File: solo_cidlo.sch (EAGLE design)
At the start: 4 parts, among them Q1 QRD1114

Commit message: Add files via upload
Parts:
- removed Q1: QRD1114, QRD1114:QRD1114
- added S1: QRD1114, QRD1114:QRD1114
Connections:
- removed net N$3: JP2.1, R1.2, R2.2
- removed net N$4: JP2.3, Q1.P$2, Q1.P$4
- new net +5V: JP2.2, R1.2, R2.2
- new net GND: JP2.3, S1.P$2, S1.P$4
- net N$1: now also S1.P$3; no longer Q1.P$3
- net N$2: now also JP2.1, S1.P$1; no longer JP2.2, Q1.P$1
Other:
- moved on the sheet: R1, R2
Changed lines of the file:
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@@
 <layers>
 <layer number="1" name="Top" color="4" fill="1" visible="no" active="no"/>
+<layer number="2" name="Route2" color="1" fill="3" visible="no" active="no"/>
+<layer number="3" name="Route3" color="4" fill="3" visible="no" active="no"/>
+<layer number="4" name="Route4" color="1" fill="4" visible="no" active="no"/>
+<layer number="5" name="Route5" color="4" fill="4" visible="no" active="no"/>
+<layer number="6" name="Route6" color="1" fill="8" visible="no" active="no"/>
+<layer number="7" name="Route7" color="4" fill="8" visible="no" active="no"/>
+<layer number="8" name="Route8" color="1" fill="2" visible="no" active="no"/>
+<layer number="9" name="Route9" color="4" fill="2" visible="no" active="no"/>
+<layer number="10" name="Route10" color="1" fill="7" visible="no" active="no"/>
+<layer number="11" name="Route11" color="4" fill="7" visible="no" active="no"/>
+<layer number="12" name="Route12" color="1" fill="5" visible="no" active="no"/>
+<layer number="13" name="Route13" color="4" fill="5" visible="no" active="no"/>
+<layer number="14" name="Route14" color="1" fill="6" visible="no" active="no"/>
+<layer number="15" name="Route15" color="4" fill="6" visible="no" active="no"/>
 <layer number="16" name="Bottom" color="1" fill="1" visible="no" active="no"/>
 <layer number="17" name="Pads" color="2" fill="1" visible="no" active="no"/>
@@
 </classes>
 <parts>
-<part name="Q1" library="QRD1114" deviceset="QRD1114" device=""/>
+<part name="S1" library="QRD1114" deviceset="QRD1114" device=""/>
 <part name="R1" library="resistor" library_urn="urn:adsk.eagle:library:348" deviceset="R-EU_" device="MELF0102W" package3d_urn="urn:adsk.eagle:package:26105/1" value="330"/>
 <part name="R2" library="resistor" library_urn="urn:adsk.eagle:library:348" deviceset="R-EU_" device="MELF0102W" package3d_urn="urn:adsk.eagle:package:26105/1" value="10 k"/>
 <part name="JP2" library="pinhead" library_urn="urn:adsk.eagle:library:325" deviceset="PINHD-1X3" device="" package3d_urn="urn:adsk.eagle:package:22458/2"/>
+<part name="GND1" library="supply1" library_urn="urn:adsk.eagle:library:371" deviceset="GND" device=""/>
+<part name="P+1" library="supply1" library_urn="urn:adsk.eagle:library:371" deviceset="+5V" device=""/>
 </parts>
 <sheets>
@@
 </plain>
 <instances>
-<instance part="Q1" gate="G$1" x="43.18" y="45.72"/>
-<instance part="R1" gate="G$1" x="40.64" y="63.5" rot="R90"/>
-<instance part="R2" gate="G$1" x="45.72" y="63.5" rot="R90"/>
+<instance part="S1" gate="G$1" x="43.18" y="38.1"/>
+<instance part="R1" gate="G$1" x="40.64" y="58.42" rot="R90"/>
+<instance part="R2" gate="G$1" x="45.72" y="58.42" rot="R90"/>
 <instance part="JP2" gate="A" x="43.18" y="81.28" rot="R90"/>
+<instance part="GND1" gate="1" x="58.42" y="73.66" rot="R90"/>
+<instance part="P+1" gate="1" x="33.02" y="66.04" rot="R90"/>
 </instances>
 <busses>
@@
 <net name="N$1" class="0">
 <segment>
-<pinref part="Q1" gate="G$1" pin="P$3"/>
+<pinref part="S1" gate="G$1" pin="P$3"/>
 <pinref part="R1" gate="G$1" pin="1"/>
-<wire x1="40.64" y1="55.88" x2="40.64" y2="58.42" width="0.1524" layer="91"/>
+<wire x1="40.64" y1="48.26" x2="40.64" y2="53.34" width="0.1524" layer="91"/>
 </segment>
 </net>
 <net name="N$2" class="0">
 <segment>
+<pinref part="S1" gate="G$1" pin="P$1"/>
+<wire x1="48.26" y1="48.26" x2="48.26" y2="50.8" width="0.1524" layer="91"/>
+<wire x1="48.26" y1="50.8" x2="48.26" y2="71.12" width="0.1524" layer="91"/>
 <pinref part="R2" gate="G$1" pin="1"/>
-<wire x1="45.72" y1="58.42" x2="48.26" y2="58.42" width="0.1524" layer="91"/>
-<pinref part="Q1" gate="G$1" pin="P$1"/>
-<wire x1="48.26" y1="58.42" x2="48.26" y2="55.88" width="0.1524" layer="91"/>
-<junction x="48.26" y="58.42"/>
-<wire x1="48.26" y1="58.42" x2="48.26" y2="71.12" width="0.1524" layer="91"/>
-<wire x1="48.26" y1="71.12" x2="43.18" y2="71.12" width="0.1524" layer="91"/>
-<pinref part="JP2" gate="A" pin="2"/>
-<wire x1="43.18" y1="71.12" x2="43.18" y2="78.74" width="0.1524" layer="91"/>
+<wire x1="45.72" y1="53.34" x2="45.72" y2="50.8" width="0.1524" layer="91"/>
+<wire x1="45.72" y1="50.8" x2="48.26" y2="50.8" width="0.1524" layer="91"/>
+<junction x="48.26" y="50.8"/>
+<pinref part="JP2" gate="A" pin="1"/>
+<wire x1="48.26" y1="71.12" x2="40.64" y2="71.12" width="0.1524" layer="91"/>
+<wire x1="40.64" y1="71.12" x2="40.64" y2="78.74" width="0.1524" layer="91"/>
 </segment>
 </net>
-<net name="N$3" class="0">
+<net name="GND" class="0">
 <segment>
-<pinref part="R1" gate="G$1" pin="2"/>
-<pinref part="R2" gate="G$1" pin="2"/>
-<wire x1="40.64" y1="68.58" x2="45.72" y2="68.58" width="0.1524" layer="91"/>
-<junction x="40.64" y="68.58"/>
-<pinref part="JP2" gate="A" pin="1"/>
-<wire x1="40.64" y1="68.58" x2="40.64" y2="78.74" width="0.1524" layer="91"/>
+<pinref part="S1" gate="G$1" pin="P$4"/>
+<wire x1="40.64" y1="27.94" x2="40.64" y2="25.4" width="0.1524" layer="91"/>
+<wire x1="40.64" y1="25.4" x2="48.26" y2="25.4" width="0.1524" layer="91"/>
+<wire x1="48.26" y1="25.4" x2="53.34" y2="25.4" width="0.1524" layer="91"/>
+<wire x1="53.34" y1="25.4" x2="53.34" y2="73.66" width="0.1524" layer="91"/>
+<wire x1="53.34" y1="73.66" x2="45.72" y2="73.66" width="0.1524" layer="91"/>
+<pinref part="S1" gate="G$1" pin="P$2"/>
+<wire x1="48.26" y1="27.94" x2="48.26" y2="25.4" width="0.1524" layer="91"/>
+<junction x="48.26" y="25.4"/>
+<pinref part="JP2" gate="A" pin="3"/>
+<wire x1="45.72" y1="73.66" x2="45.72" y2="78.74" width="0.1524" layer="91"/>
+<pinref part="GND1" gate="1" pin="GND"/>
+<wire x1="55.88" y1="73.66" x2="53.34" y2="73.66" width="0.1524" layer="91"/>
+<junction x="53.34" y="73.66"/>
 </segment>
 </net>
-<net name="N$4" class="0">
+<net name="+5V" class="0">
 <segment>
-<pinref part="Q1" gate="G$1" pin="P$4"/>
-<wire x1="40.64" y1="35.56" x2="40.64" y2="33.02" width="0.1524" layer="91"/>
-<wire x1="40.64" y1="33.02" x2="48.26" y2="33.02" width="0.1524" layer="91"/>
-<wire x1="48.26" y1="33.02" x2="53.34" y2="33.02" width="0.1524" layer="91"/>
-<wire x1="53.34" y1="33.02" x2="53.34" y2="73.66" width="0.1524" layer="91"/>
-<wire x1="53.34" y1="73.66" x2="45.72" y2="73.66" width="0.1524" layer="91"/>
-<pinref part="Q1" gate="G$1" pin="P$2"/>
-<wire x1="48.26" y1="35.56" x2="48.26" y2="33.02" width="0.1524" layer="91"/>
-<junction x="48.26" y="33.02"/>
-<pinref part="JP2" gate="A" pin="3"/>
-<wire x1="45.72" y1="73.66" x2="45.72" y2="78.74" width="0.1524" layer="91"/>
+<pinref part="JP2" gate="A" pin="2"/>
+<wire x1="43.18" y1="78.74" x2="43.18" y2="66.04" width="0.1524" layer="91"/>
+<wire x1="43.18" y1="66.04" x2="45.72" y2="66.04" width="0.1524" layer="91"/>
+<pinref part="R2" gate="G$1" pin="2"/>
+<wire x1="45.72" y1="66.04" x2="45.72" y2="63.5" width="0.1524" layer="91"/>
+<pinref part="R1" gate="G$1" pin="2"/>
+<wire x1="43.18" y1="66.04" x2="40.64" y2="66.04" width="0.1524" layer="91"/>
+<wire x1="40.64" y1="66.04" x2="40.64" y2="63.5" width="0.1524" layer="91"/>
+<junction x="43.18" y="66.04"/>
+<pinref part="P+1" gate="1" pin="+5V"/>
+<wire x1="35.56" y1="66.04" x2="40.64" y2="66.04" width="0.1524" layer="91"/>
+<junction x="40.64" y="66.04"/>
 </segment>
 </net>

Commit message: Add files via upload
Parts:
- added LED1: (no value), led:LEDCHIPLED_0603
- added R3: 330, resistor:R-EU_R0201
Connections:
- net N$1 renamed IL1
- net N$2 renamed S1
- new net KL1: LED1.A, R3.1
- net +5V: now also R3.2
- net GND: now also LED1.C
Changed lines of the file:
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@@
 <setting verticaltext="up"/>
 </settings>
-<grid distance="0.1" unitdist="inch" unit="inch" style="lines" multiple="1" display="yes" altdistance="0.01" altunitdist="inch" altunit="inch"/>
+<grid distance="0.1" unitdist="inch" unit="inch" style="lines" multiple="1" display="no" altdistance="0.01" altunitdist="inch" altunit="inch"/>
 <layers>
-<layer number="1" name="Top" color="4" fill="1" visible="no" active="no"/>
-<layer number="2" name="Route2" color="1" fill="3" visible="no" active="no"/>
-<layer number="3" name="Route3" color="4" fill="3" visible="no" active="no"/>
-<layer number="4" name="Route4" color="1" fill="4" visible="no" active="no"/>
-<layer number="5" name="Route5" color="4" fill="4" visible="no" active="no"/>
-<layer number="6" name="Route6" color="1" fill="8" visible="no" active="no"/>
-<layer number="7" name="Route7" color="4" fill="8" visible="no" active="no"/>
-<layer number="8" name="Route8" color="1" fill="2" visible="no" active="no"/>
-<layer number="9" name="Route9" color="4" fill="2" visible="no" active="no"/>
-<layer number="10" name="Route10" color="1" fill="7" visible="no" active="no"/>
-<layer number="11" name="Route11" color="4" fill="7" visible="no" active="no"/>
-<layer number="12" name="Route12" color="1" fill="5" visible="no" active="no"/>
-<layer number="13" name="Route13" color="4" fill="5" visible="no" active="no"/>
-<layer number="14" name="Route14" color="1" fill="6" visible="no" active="no"/>
-<layer number="15" name="Route15" color="4" fill="6" visible="no" active="no"/>
-<layer number="16" name="Bottom" color="1" fill="1" visible="no" active="no"/>
-<layer number="17" name="Pads" color="2" fill="1" visible="no" active="no"/>
-<layer number="18" name="Vias" color="2" fill="1" visible="no" active="no"/>
-<layer number="19" name="Unrouted" color="6" fill="1" visible="no" active="no"/>
-<layer number="20" name="Dimension" color="15" fill="1" visible="no" active="no"/>
-<layer number="21" name="tPlace" color="7" fill="1" visible="no" active="no"/>
-<layer number="22" name="bPlace" color="7" fill="1" visible="no" active="no"/>
-<layer number="23" name="tOrigins" color="15" fill="1" visible="no" active="no"/>
-<layer number="24" name="bOrigins" color="15" fill="1" visible="no" active="no"/>
-<layer number="25" name="tNames" color="7" fill="1" visible="no" active="no"/>
-<layer number="26" name="bNames" color="7" fill="1" visible="no" active="no"/>
-<layer number="27" name="tValues" color="7" fill="1" visible="no" active="no"/>
-<layer number="28" name="bValues" color="7" fill="1" visible="no" active="no"/>
+<layer number="1" name="Top" color="4" fill="1" visible="yes" active="no"/>
+<layer number="2" name="Route2" color="1" fill="3" visible="yes" active="no"/>
+<layer number="3" name="Route3" color="4" fill="3" visible="yes" active="no"/>
+<layer number="4" name="Route4" color="1" fill="4" visible="yes" active="no"/>
+<layer number="5" name="Route5" color="4" fill="4" visible="yes" active="no"/>
+<layer number="6" name="Route6" color="1" fill="8" visible="yes" active="no"/>
+<layer number="7" name="Route7" color="4" fill="8" visible="yes" active="no"/>
+<layer number="8" name="Route8" color="1" fill="2" visible="yes" active="no"/>
+<layer number="9" name="Route9" color="4" fill="2" visible="yes" active="no"/>
+<layer number="10" name="Route10" color="1" fill="7" visible="yes" active="no"/>
+<layer number="11" name="Route11" color="4" fill="7" visible="yes" active="no"/>
+<layer number="12" name="Route12" color="1" fill="5" visible="yes" active="no"/>
+<layer number="13" name="Route13" color="4" fill="5" visible="yes" active="no"/>
+<layer number="14" name="Route14" color="1" fill="6" visible="yes" active="no"/>
+<layer number="15" name="Route15" color="4" fill="6" visible="yes" active="no"/>
+<layer number="16" name="Bottom" color="1" fill="1" visible="yes" active="no"/>
+<layer number="17" name="Pads" color="2" fill="1" visible="yes" active="no"/>
+<layer number="18" name="Vias" color="2" fill="1" visible="yes" active="no"/>
+<layer number="19" name="Unrouted" color="6" fill="1" visible="yes" active="no"/>
+<layer number="20" name="Dimension" color="24" fill="1" visible="yes" active="no"/>
+<layer number="21" name="tPlace" color="7" fill="1" visible="yes" active="no"/>
+<layer number="22" name="bPlace" color="7" fill="1" visible="yes" active="no"/>
+<layer number="23" name="tOrigins" color="15" fill="1" visible="yes" active="no"/>
+<layer number="24" name="bOrigins" color="15" fill="1" visible="yes" active="no"/>
+<layer number="25" name="tNames" color="7" fill="1" visible="yes" active="no"/>
+<layer number="26" name="bNames" color="7" fill="1" visible="yes" active="no"/>
+<layer number="27" name="tValues" color="7" fill="1" visible="yes" active="no"/>
+<layer number="28" name="bValues" color="7" fill="1" visible="yes" active="no"/>
 <layer number="29" name="tStop" color="7" fill="3" visible="no" active="no"/>
 <layer number="30" name="bStop" color="7" fill="6" visible="no" active="no"/>
@@
 <layer number="35" name="tGlue" color="7" fill="4" visible="no" active="no"/>
 <layer number="36" name="bGlue" color="7" fill="5" visible="no" active="no"/>
-<layer number="37" name="tTest" color="7" fill="1" visible="no" active="no"/>
-<layer number="38" name="bTest" color="7" fill="1" visible="no" active="no"/>
+<layer number="37" name="tTest" color="7" fill="1" visible="yes" active="no"/>
+<layer number="38" name="bTest" color="7" fill="1" visible="yes" active="no"/>
 <layer number="39" name="tKeepout" color="4" fill="11" visible="no" active="no"/>
 <layer number="40" name="bKeepout" color="1" fill="11" visible="no" active="no"/>
@@
 <layer number="44" name="Drills" color="7" fill="1" visible="no" active="no"/>
 <layer number="45" name="Holes" color="7" fill="1" visible="no" active="no"/>
-<layer number="46" name="Milling" color="3" fill="1" visible="no" active="no"/>
-<layer number="47" name="Measures" color="7" fill="1" visible="no" active="no"/>
-<layer number="48" name="Document" color="7" fill="1" visible="no" active="no"/>
-<layer number="49" name="Reference" color="7" fill="1" visible="no" active="no"/>
-<layer number="51" name="tDocu" color="7" fill="1" visible="no" active="no"/>
-<layer number="52" name="bDocu" color="7" fill="1" visible="no" active="no"/>
+<layer number="46" name="Milling" color="3" fill="1" visible="yes" active="no"/>
+<layer number="47" name="Measures" color="7" fill="1" visible="yes" active="no"/>
+<layer number="48" name="Document" color="7" fill="1" visible="yes" active="no"/>
+<layer number="49" name="Reference" color="7" fill="1" visible="yes" active="no"/>
+<layer number="51" name="tDocu" color="7" fill="1" visible="yes" active="no"/>
+<layer number="52" name="bDocu" color="7" fill="1" visible="yes" active="no"/>
 <layer number="88" name="SimResults" color="9" fill="1" visible="yes" active="yes"/>
 <layer number="89" name="SimProbes" color="9" fill="1" visible="yes" active="yes"/>
@@
 <part name="GND1" library="supply1" library_urn="urn:adsk.eagle:library:371" deviceset="GND" device=""/>
 <part name="P+1" library="supply1" library_urn="urn:adsk.eagle:library:371" deviceset="+5V" device=""/>
+<part name="LED1" library="led" library_urn="urn:adsk.eagle:library:259" deviceset="LED" device="CHIPLED_0603" package3d_urn="urn:adsk.eagle:package:15822/2"/>
+<part name="R3" library="resistor" library_urn="urn:adsk.eagle:library:348" deviceset="R-EU_" device="R0201" package3d_urn="urn:adsk.eagle:package:26117/1" value="330"/>
 </parts>
 <sheets>
@@
 <instance part="JP2" gate="A" x="43.18" y="81.28" rot="R90"/>
 <instance part="GND1" gate="1" x="58.42" y="73.66" rot="R90"/>
-<instance part="P+1" gate="1" x="33.02" y="66.04" rot="R90"/>
+<instance part="P+1" gate="1" x="22.86" y="66.04" rot="R90"/>
+<instance part="LED1" gate="G$1" x="33.02" y="40.64"/>
+<instance part="R3" gate="G$1" x="33.02" y="58.42" rot="R90"/>
 </instances>
 <busses>
 </busses>
 <nets>
-<net name="N$1" class="0">
+<net name="IL1" class="0">
 <segment>
 <pinref part="S1" gate="G$1" pin="P$3"/>
@@
 </segment>
 </net>
-<net name="N$2" class="0">
+<net name="S1" class="0">
 <segment>
 <pinref part="S1" gate="G$1" pin="P$1"/>
@@
 <wire x1="48.26" y1="71.12" x2="40.64" y2="71.12" width="0.1524" layer="91"/>
 <wire x1="40.64" y1="71.12" x2="40.64" y2="78.74" width="0.1524" layer="91"/>
+<label x="40.64" y="71.12" size="1.778" layer="95" rot="R90"/>
 </segment>
 </net>
@@
 <wire x1="55.88" y1="73.66" x2="53.34" y2="73.66" width="0.1524" layer="91"/>
 <junction x="53.34" y="73.66"/>
+<pinref part="LED1" gate="G$1" pin="C"/>
+<wire x1="33.02" y1="35.56" x2="33.02" y2="25.4" width="0.1524" layer="91"/>
+<wire x1="33.02" y1="25.4" x2="40.64" y2="25.4" width="0.1524" layer="91"/>
+<junction x="40.64" y="25.4"/>
 </segment>
 </net>
@@
 <junction x="43.18" y="66.04"/>
 <pinref part="P+1" gate="1" pin="+5V"/>
-<wire x1="35.56" y1="66.04" x2="40.64" y2="66.04" width="0.1524" layer="91"/>
+<wire x1="25.4" y1="66.04" x2="33.02" y2="66.04" width="0.1524" layer="91"/>
 <junction x="40.64" y="66.04"/>
+<pinref part="R3" gate="G$1" pin="2"/>
+<wire x1="33.02" y1="66.04" x2="40.64" y2="66.04" width="0.1524" layer="91"/>
+<wire x1="33.02" y1="66.04" x2="33.02" y2="63.5" width="0.1524" layer="91"/>
+<junction x="33.02" y="66.04"/>
 </segment>
 </net>
+<net name="KL1" class="0">
+<segment>
+<pinref part="R3" gate="G$1" pin="1"/>
+<pinref part="LED1" gate="G$1" pin="A"/>
+<wire x1="33.02" y1="53.34" x2="33.02" y2="43.18" width="0.1524" layer="91"/>
+</segment>
+</net>

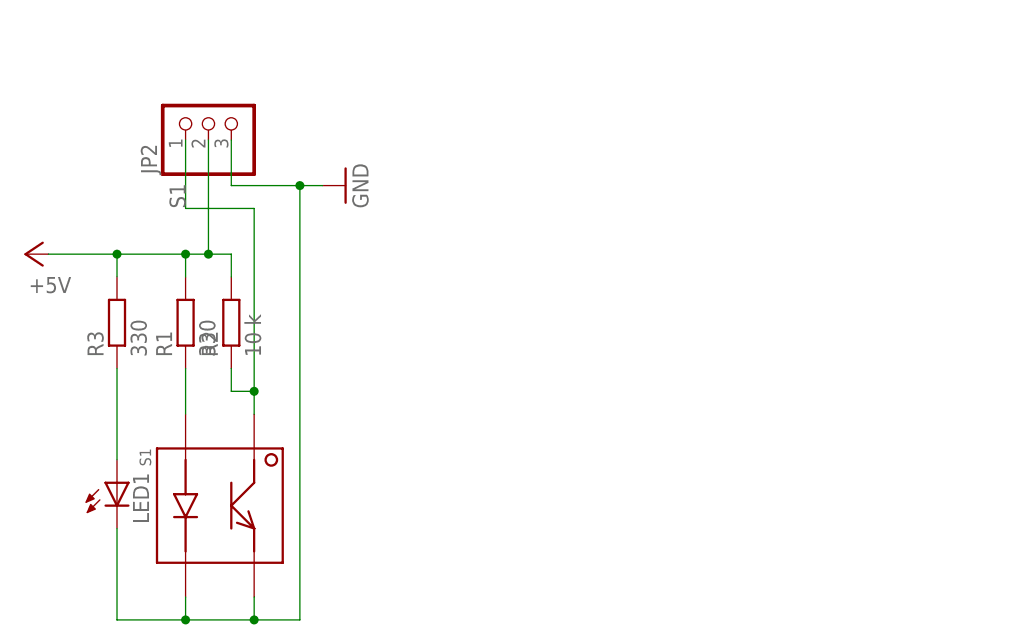
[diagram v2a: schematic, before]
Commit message: Prepare PCB to manufacturing
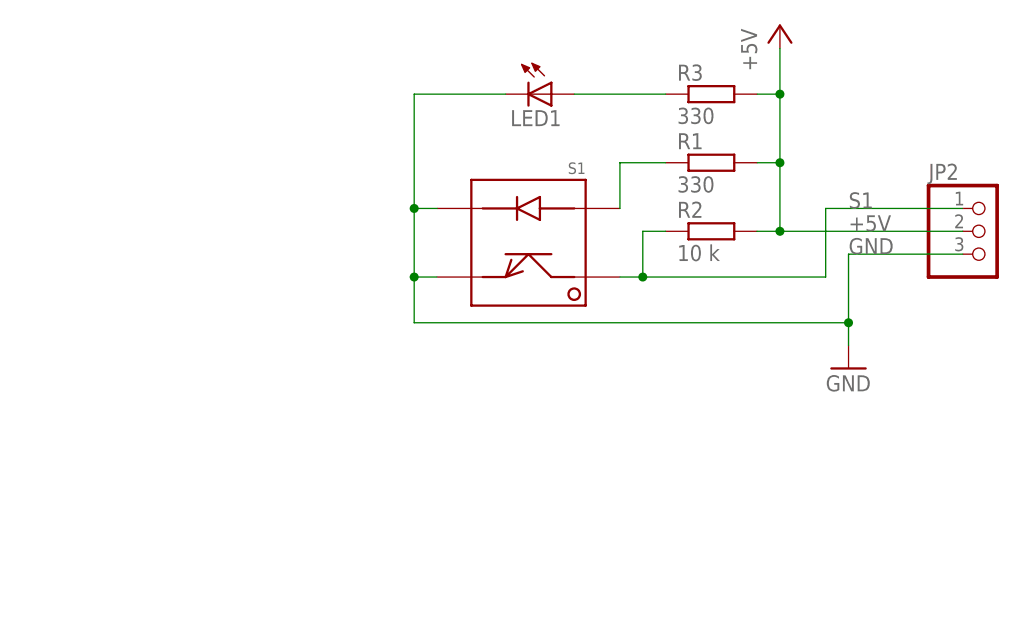
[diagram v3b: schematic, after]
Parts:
- R3: device resistor:R-EU_R0201 -> resistor:R-EU_R0603
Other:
- moved on the sheet: JP2, LED1, R1, R2, R3, S1
